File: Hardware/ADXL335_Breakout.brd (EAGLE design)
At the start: 17.8 x 17.8 mm, 10 parts

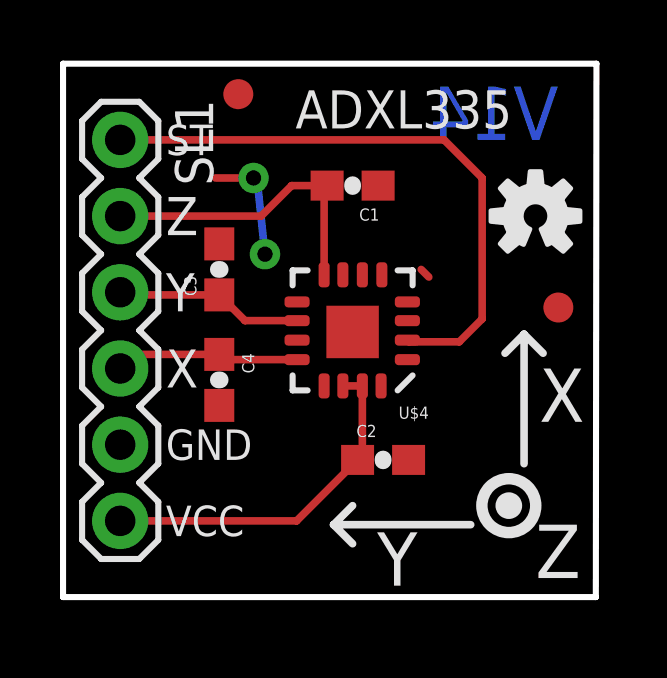
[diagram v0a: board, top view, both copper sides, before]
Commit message: T-Res change/ Removed Traces/Pour Dimension Change
Added t restrict to a few pins for better solder flow,  also removed
traces on the ground for the bottom and top copper as it was
unnecessary.  Also made the top copper pour dimension match the bottom
copper pour
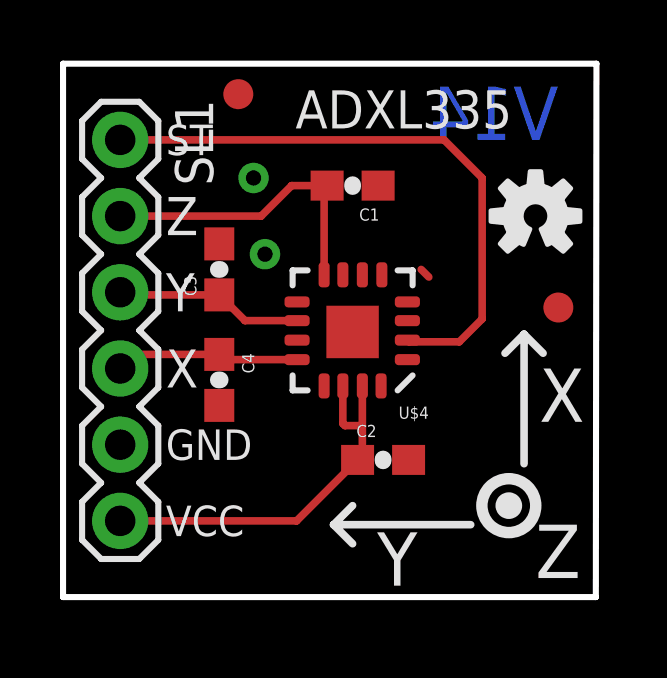
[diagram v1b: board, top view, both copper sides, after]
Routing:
- net GND: track 4.24 -> 0.36 mm
- net VCC: track 12.1 -> 13.4 mm
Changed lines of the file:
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@@
 <layer number="27" name="tValues" color="7" fill="1" visible="no" active="yes"/>
 <layer number="28" name="bValues" color="7" fill="1" visible="no" active="yes"/>
-<layer number="29" name="tStop" color="7" fill="3" visible="yes" active="yes"/>
+<layer number="29" name="tStop" color="7" fill="3" visible="no" active="yes"/>
 <layer number="30" name="bStop" color="7" fill="6" visible="no" active="yes"/>
 <layer number="31" name="tCream" color="7" fill="4" visible="no" active="yes"/>
@@
 <layer number="39" name="tKeepout" color="4" fill="11" visible="no" active="yes"/>
 <layer number="40" name="bKeepout" color="1" fill="11" visible="no" active="yes"/>
-<layer number="41" name="tRestrict" color="4" fill="10" visible="yes" active="yes"/>
+<layer number="41" name="tRestrict" color="4" fill="10" visible="no" active="yes"/>
 <layer number="42" name="bRestrict" color="1" fill="10" visible="no" active="yes"/>
 <layer number="43" name="vRestrict" color="2" fill="10" visible="no" active="yes"/>
@@
 <layer number="106" name="bPlate" color="7" fill="1" visible="no" active="yes"/>
 <layer number="107" name="Crop" color="7" fill="1" visible="no" active="yes"/>
-<layer number="108" name="tplace-old" color="10" fill="1" visible="yes" active="yes"/>
-<layer number="109" name="ref-old" color="11" fill="1" visible="yes" active="yes"/>
+<layer number="108" name="tplace-old" color="10" fill="1" visible="no" active="yes"/>
+<layer number="109" name="ref-old" color="11" fill="1" visible="no" active="yes"/>
 <layer number="116" name="Patch_BOT" color="9" fill="4" visible="no" active="yes"/>
 <layer number="121" name="_tsilk" color="7" fill="1" visible="no" active="yes"/>
@@
 <layer number="144" name="Drill_legend" color="7" fill="1" visible="no" active="yes"/>
 <layer number="151" name="HeatSink" color="7" fill="1" visible="no" active="yes"/>
-<layer number="199" name="Contour" color="7" fill="1" visible="yes" active="yes"/>
+<layer number="199" name="Contour" color="7" fill="1" visible="no" active="yes"/>
 <layer number="200" name="200bmp" color="1" fill="10" visible="no" active="no"/>
 <layer number="201" name="201bmp" color="2" fill="1" visible="no" active="no"/>
@@
 <text x="15.748" y="0.635" size="1.778" layer="21" font="vector" ratio="15">Z</text>
 <text x="16.51" y="15.24" size="1.778" layer="16" font="vector" ratio="15" rot="MR0">V14</text>
+<rectangle x1="9.525" y1="10.668" x2="9.779" y2="10.795" layer="41"/>
+<rectangle x1="10.16" y1="10.668" x2="10.414" y2="10.795" layer="41"/>
+<rectangle x1="10.922" y1="10.668" x2="11.049" y2="10.795" layer="41"/>
+<rectangle x1="11.049" y1="10.16" x2="11.43" y2="11.176" layer="41"/>
+<rectangle x1="11.176" y1="10.16" x2="11.557" y2="11.303" layer="41"/>
+<rectangle x1="10.922" y1="11.176" x2="11.303" y2="11.43" layer="41"/>
 </plain>
 <attributes>
@@
 <contactref element="U$4" pad="3"/>
 <contactref element="U$4" pad="7"/>
-<wire x1="6.477" y1="13.843" x2="6.35" y2="13.97" width="0.254" layer="16"/>
-<wire x1="6.35" y1="13.97" x2="5.08" y2="13.97" width="0.254" layer="1"/>
 <via x="6.731" y="11.43" extent="1-16" drill="0.508"/>
 <via x="6.35" y="13.97" extent="1-16" drill="0.508"/>
@@
 <vertex x="0" y="0"/>
 </polygon>
-<polygon width="0.2032" layer="1" isolate="0.3048">
+<polygon width="0.2032" layer="1">
 <vertex x="0" y="0"/>
 <vertex x="17.78" y="0"/>
@@
 </polygon>
 <wire x1="12.192" y1="10.668" x2="11.938" y2="10.922" width="0.254" layer="1"/>
-<wire x1="6.731" y1="11.43" x2="6.477" y2="13.843" width="0.254" layer="16"/>
 </signal>
 <signal name="VCC">
@@
 <contactref element="U$4" pad="14"/>
 <contactref element="U$4" pad="15"/>
-<wire x1="9.977" y1="7.0384" x2="9.327" y2="7.0384" width="0.254" layer="1"/>
 <wire x1="9.818" y1="4.572" x2="9.818" y2="4.738" width="0.254" layer="1"/>
 <wire x1="1.905" y1="2.54" x2="7.786" y2="2.54" width="0.254" layer="1"/>
 <wire x1="7.786" y1="2.54" x2="9.818" y2="4.572" width="0.254" layer="1"/>
-<wire x1="9.977" y1="7.0384" x2="9.977" y2="4.731" width="0.254" layer="1"/>
+<wire x1="9.977" y1="7.0384" x2="9.977" y2="5.715" width="0.254" layer="1"/>
+<wire x1="9.977" y1="5.715" x2="9.977" y2="4.731" width="0.254" layer="1"/>
 <wire x1="9.977" y1="4.731" x2="9.818" y2="4.572" width="0.254" layer="1"/>
+<wire x1="9.327" y1="7.0384" x2="9.327" y2="5.786" width="0.254" layer="1"/>
+<wire x1="9.327" y1="5.786" x2="9.398" y2="5.715" width="0.254" layer="1"/>
+<wire x1="9.398" y1="5.715" x2="9.977" y2="5.715" width="0.254" layer="1"/>
 </signal>
 <signal name="XOUT">

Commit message: Rev Dimension/Silk Design and more
A redo on the dimension of the PCB, Added a new axis to the silk,
revised the bplace with new aesthetics.  Also standoff holes were added.
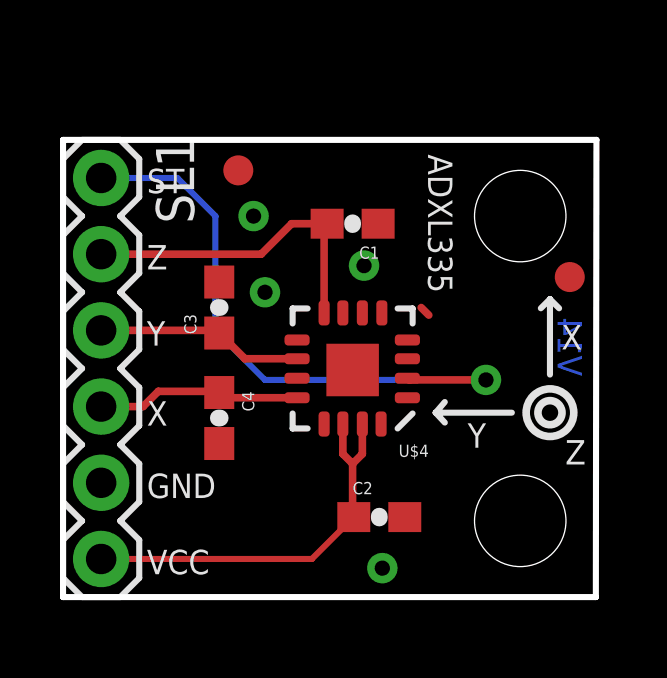
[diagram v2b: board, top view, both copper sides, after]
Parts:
- removed U$2: LOGO-SFE, SparkFun:SFE-NEW-WEBLOGO
- added U$6, U$7: (no value), SparkFun:STAND-OFF-TIGHT
- added U$8: (no value), SparkFun-Aesthetics:SFE_LOGO_NAME_.1
- U$5: value OSHW-LOGOS -> (none)
- moved U$5 11.8 mm to (5.08, 7.62), flipped to the bottom, turned to 90 degrees
- moved U$1 2.54 mm to (5.84, 14.2)
- moved C2 1.91 mm to (10.5, 2.67)
- moved SL1 1.42 mm to (1.27, 14.0)
- moved C3 1.27 mm to (5.21, 9.65)
- moved U$4 1.27 mm to (9.65, 7.62)
- moved C1 1.27 mm to (9.65, 12.4)
- moved C4 1.27 mm to (5.21, 5.97)
- moved U$3 1.09 mm to (16.9, 10.7)
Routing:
- net XOUT: track 6.16 -> 6.83 mm
- net YOUT: track 6.29 -> 6.92 mm
- net ZOUT: track 10.3 -> 11.0 mm
- net ST: track 20.1 -> 20.5 mm, vias 0 -> 1
- net GND: track 0.36 -> 0.41 mm, vias 2 -> 4
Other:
- board size 17.8 x 17.8 mm -> 17.8 x 15.2 mm
- board text added: "Accelerometer"
- board text added: "Tri-Axis"

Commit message: moved fiducials
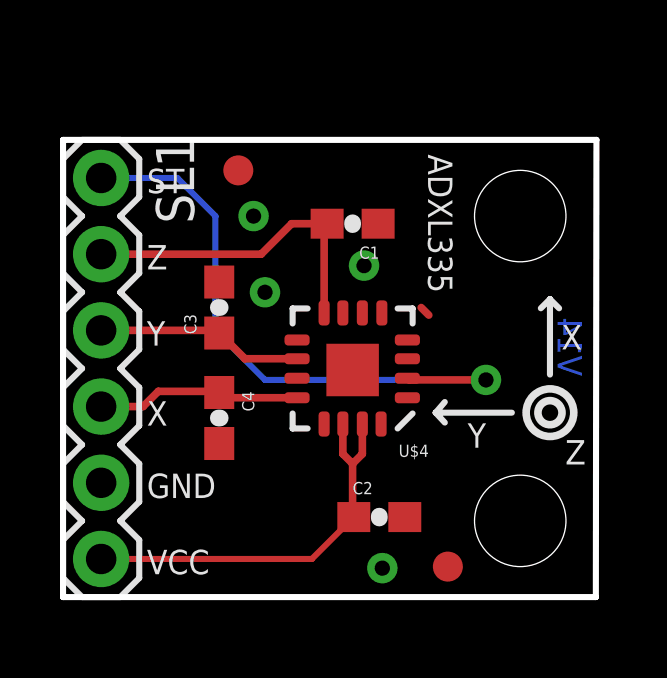
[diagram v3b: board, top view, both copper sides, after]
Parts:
- moved U$3 10.5 mm to (12.8, 1.02)
